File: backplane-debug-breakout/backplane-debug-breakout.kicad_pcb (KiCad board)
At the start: 2 copper layers, 11 parts, among them J1 Conn_02x08_Odd_Even, J2 Conn_01x04, J3 Conn_01x01_Socket, J4 Conn_01x01_Socket, J5 Conn_01x04, SW1 SW_Push, SW2 SW_DPST_x2

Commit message: added to pcb
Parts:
- moved SW2 43.7 mm to (136.0, 68.0)
- moved SW1 35.8 mm to (129.0, 69.4), turned to 90 degrees
- moved J2 15.9 mm to (115.0, 82.9)
- moved D1 12.7 mm to (118.8, 65.0)
- moved F2 12.5 mm to (118.5, 72.5)
- moved J5 8.65 mm to (109.8, 61.5), turned to -90 degrees
- moved J1 0.95 mm to (105.0, 70.2)
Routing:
- net /SD: track 0.71 -> 48.0 mm
- net /CAN_H: track 0.00 -> 17.5 mm
- net /OPD_SCL: track 0.00 -> 14.7 mm
- net Net-(D1-K): track 0.00 -> 13.4 mm
- net Net-(J1-Pin_10): track 0.00 -> 9.26 mm
- net /CAN_L: track 0.00 -> 8.82 mm
- added copper zone on B.Cu, net GND
- added copper zone on F.Cu, net GND

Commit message: updated pcb
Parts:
- moved PCB1 1.01 mm to (161.8, 62.0)
- moved vCAN 0.60 mm to (126.8, 105.4)
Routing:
- net /C3-UART-TX: track 0.00 -> 79.0 mm, vias 0 -> 1
- net /C3-UART-RX: track 0.00 -> 65.4 mm
- net Net-(D1-A): track 0.00 -> 42.7 mm, vias 0 -> 1
- net Net-(J1-Pin_10): track 9.26 -> 14.3 mm

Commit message: edited PBC
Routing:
- net Net-(PCB1-3V3): track 0.00 -> 2.54 mm
- net /C3-UART-TX: track 79.0 -> 80.6 mm
- net /C3-UART-RX: track 65.4 -> 66.4 mm
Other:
- board outline added: 65 x 50.5 mm
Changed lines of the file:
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@@
 		(tags "banana socket")
 		(property "Reference" "J4"
-			(at 0 -6.5 90)
+			(at 4 -5.5 90)
 			(layer "F.SilkS")
 			(effects
@@
 			)
 		)
-		(sheetname "Root")
-		(sheetfile "backplane-debug-breakout.kicad_sch")
 		(attr through_hole)
-		(fp_rect
-			(start 0 0)
+		(fp_line
+			(start 0 21)
 			(end 12.7 21)
 			(stroke
@@
 				(type default)
 			)
-			(fill none)
 			(layer "F.SilkS")
 		)
-		(fp_rect
-			(start 0 0)
-			(end 12.7 21)
+		(fp_line
+			(start 0 0.5)
+			(end 0 8)
 			(stroke
 				(width 0.1)
 				(type default)
 			)
-			(fill none)
-			(layer "F.CrtYd")
-		)
-		(fp_circle
-			(center 0 19.77)
-			(end 0.762 19.77)
-			(stroke
-				(width 0.05)
-				(type default)
-			)
-			(fill none)
-			(layer "F.CrtYd")
-		)
-		(fp_circle
-			(center 12.7 19.77)
-			(end 13.462 19.77)
-			(stroke
-				(width 0.05)
-				(type default)
-			)
-			(fill none)
-			(layer "F.CrtYd")
-		)
-		(fp_circle
-			(center 0 17.23)
-			(end 0.762 17.23)
-			(stroke
-				(width 0.05)
-				(type default)
-			)
-			(fill none)
-			(layer "F.CrtYd")
-		)
-		(fp_circle
-			(center 12.7 17.23)
-			(end 13.462 17.23)
-			(stroke
-				(width 0.05)
-				(type default)
-			)
-			(fill none)
-			(layer "F.CrtYd")
-		)
-		(fp_circle
-			(center 0 14.69)
-			(end 0.762 14.69)
-			(stroke
-				(width 0.05)
-				(type default)
-			)
-			(fill none)
-			(layer "F.CrtYd")
-		)
-		(fp_circle
-			(center 12.7 14.69)
-			(end 13.462 14.69)
-			(stroke
-				(width 0.05)
-				(type default)
-			)
-			(fill none)
-			(layer "F.CrtYd")
+			(layer "F.SilkS")
 		)
-		(fp_circle
-			(center 0 12.15)
-			(end 0.762 12.15)
+		(fp_line
+			(start 12.7 0.5)
+			(end 12.7 8)
 			(stroke
-				(width 0.05)
+				(width 0.1)
 				(type default)
 			)
-			(fill none)
-			(layer "F.CrtYd")
+			(layer "F.SilkS")
 		)
-		(fp_circle
-			(center 12.7 12.15)
-			(end 13.462 12.15)
+		(fp_line
+			(start 0 0)
+			(end 12.7 0)
 			(stroke
-				(width 0.05)
+				(width 0.1)
 				(type default)
 			)
-			(fill none)
-			(layer "F.CrtYd")
+			(layer "Cmts.User")
 		)
-		(fp_circle
-			(center 0 9.61)
-			(end 0.762 9.61)
+		(fp_rect
+			(start -2 -1)
+			(end 14.7 22)
 			(stroke
-				(width 0.05)
+				(width 0.1)
 				(type default)
 			)
@@
 			(layer "F.CrtYd")
 		)
-		(fp_circle
-			(center 12.7 9.61)
-			(end 13.462 9.61)
-			(stroke
-				(width 0.05)
-				(type default)
+		(fp_text user "PCB Edge"
+			(at 3.5 1.5 -90)
+			(unlocked yes)
+			(layer "Cmts.User")
+			(effects
+				(font
+					(size 1 1)
+					(thickness 0.15)
+				)
+				(justify left bottom)
 			)
-			(fill none)
-			(layer "F.CrtYd")
 		)
 		(fp_text user "${REFERENCE}"
@@
 			)
 		)
-		(pad "P1" thru_hole circle
+		(pad "P1" smd rect
 			(at 0 9.61 270)
-			(size 1.524 1.524)
-			(drill 0.762)
-			(layers "*.Cu" "*.Mask")
-			(remove_unused_layers no)
+			(size 2 2)
+			(layers "F.Cu" "F.Paste" "F.Mask")
 			(net 16 "unconnected-(PCB1-RESET#-PadP1)")
 			(pinfunction "RESET#")
 			(pintype "input+no_connect")
 		)
-		(pad "P2" thru_hole circle
+		(pad "P2" smd rect
 			(at 0 12.15 270)
-			(size 1.524 1.524)
-			(drill 0.762)
-			(layers "*.Cu" "*.Mask")
-			(remove_unused_layers no)
+			(size 2 2)
+			(layers "F.Cu" "F.Paste" "F.Mask")
 			(net 17 "Net-(PCB1-3V3)")
 			(pinfunction "3V3")
 			(pintype "power_out")
 		)
-		(pad "P3" thru_hole circle
+		(pad "P3" smd rect
 			(at 0 14.69 270)
-			(size 1.524 1.524)
-			(drill 0.762)
-			(layers "*.Cu" "*.Mask")
-			(remove_unused_layers no)
+			(size 2 2)
+			(layers "F.Cu" "F.Paste" "F.Mask")
 			(net 17 "Net-(PCB1-3V3)")
 			(pinfunction "VIO")
 			(pintype "power_in")
 		)
-		(pad "P4" thru_hole circle
+		(pad "P4" smd rect
 			(at 0 17.23 270)
-			(size 1.524 1.524)
-			(drill 0.762)
-			(layers "*.Cu" "*.Mask")
-			(remove_unused_layers no)
+			(size 2 2)
+			(layers "F.Cu" "F.Paste" "F.Mask")
 			(net 6 "GND")
 			(pinfunction "GND")
 			(pintype "power_in")
 		)
-		(pad "P5" thru_hole circle
+		(pad "P5" smd rect
 			(at 0 19.77 270)
-			(size 1.524 1.524)
-			(drill 0.762)
-			(layers "*.Cu" "*.Mask")
-			(remove_unused_layers no)
+			(size 2 2)
+			(layers "F.Cu" "F.Paste" "F.Mask")
 			(net 20 "unconnected-(PCB1-VBUS-PadP5)")
 			(pinfunction "VBUS")
 			(pintype "power_out+no_connect")
 		)
-		(pad "P6" thru_hole circle
+		(pad "P6" smd rect
 			(at 12.7 19.77 270)
-			(size 1.524 1.524)
-			(drill 0.762)
-			(layers "*.Cu" "*.Mask")
-			(remove_unused_layers no)
+			(size 2 2)
+			(layers "F.Cu" "F.Paste" "F.Mask")
 			(net 18 "unconnected-(PCB1-CB0-PadP6)")
 			(pinfunction "CB0")
 			(pintype "bidirectional+no_connect")
 		)
-		(pad "P7" thru_hole circle
+		(pad "P7" smd rect
 			(at 12.7 17.23 270)
-			(size 1.524 1.524)
-			(drill 0.762)
-			(layers "*.Cu" "*.Mask")
-			(remove_unused_layers no)
+			(size 2 2)
+			(layers "F.Cu" "F.Paste" "F.Mask")
 			(net 5 "/C3-UART-TX")
 			(pinfunction "TXD")
 			(pintype "output")
 		)
-		(pad "P8" thru_hole circle
+		(pad "P8" smd rect
 			(at 12.7 14.69 270)
-			(size 1.524 1.524)
-			(drill 0.762)
-			(layers "*.Cu" "*.Mask")
-			(remove_unused_layers no)
+			(size 2 2)
+			(layers "F.Cu" "F.Paste" "F.Mask")
 			(net 19 "unconnected-(PCB1-RTS#-PadP8)")
 			(pinfunction "RTS#")
 			(pintype "output+no_connect")
 		)
-		(pad "P9" thru_hole circle
+		(pad "P9" smd rect
 			(at 12.7 12.15 270)
-			(size 1.524 1.524)
-			(drill 0.762)
-			(layers "*.Cu" "*.Mask")
-			(remove_unused_layers no)
+			(size 2 2)
+			(layers "F.Cu" "F.Paste" "F.Mask")
 			(net 8 "/C3-UART-RX")
 			(pinfunction "RXD")
 			(pintype "input")
 		)
-		(pad "P10" thru_hole circle
+		(pad "P10" smd rect
 			(at 12.7 9.61 270)
-			(size 1.524 1.524)
-			(drill 0.762)
-			(layers "*.Cu" "*.Mask")
-			(remove_unused_layers no)
+			(size 2 2)
+			(layers "F.Cu" "F.Paste" "F.Mask")
 			(net 21 "unconnected-(PCB1-CTS#-PadP10)")
 			(pinfunction "CTS#")
@@
 		)
 	)
-	(gr_rect
-		(start 97 59)
-		(end 162 109.5)
-		(stroke
-			(width 0.2)
-			(type default)
-		)
-		(fill none)
-		(layer "F.Cu")
-		(net 4)
-	)
 	(gr_line
 		(start 114.96 82.92)
@@
 		(net 7)
 	)
+	(gr_rect
+		(start 97 59)
+		(end 162 109.5)
+		(stroke
+			(width 0.2)
+			(type default)
+		)
+		(fill none)
+		(layer "Edge.Cuts")
+	)
 	(segment
 		(start 113 65)
@@
 	(segment
 		(start 144.54 74.7)
-		(end 124.24 95)
+		(end 144.54 77.46)
 		(width 0.4)
 		(layer "F.Cu")
@@
 	)
 	(segment
-		(start 124.24 95)
+		(start 127 95)
 		(end 100.5 95)
 		(width 0.4)
@@
 		(net 5)
 	)
+	(segment
+		(start 144.54 77.46)
+		(end 127 95)
+		(width 0.4)
+		(layer "F.Cu")
+		(net 5)
+	)
 	(via
 		(at 100.5 73)
@@
 	)
 	(segment
-		(start 149.62 73.62)
-		(end 148.5 72.5)
+		(start 149.62 74.7)
+		(end 149.62 72.62)
 		(width 0.4)
 		(layer "F.Cu")
@@
 	)
 	(segment
-		(start 112 63.5)
-		(end 112 68.26)
+		(start 149 72)
+		(end 141.5 72)
 		(width 0.4)
 		(layer "F.Cu")
@@
 	)
 	(segment
-		(start 148.5 72.5)
-		(end 141 72.5)
+		(start 126.5 73)
+		(end 126.5 62)
 		(width 0.4)
 		(layer "F.Cu")
@@
 	)
 	(segment
-		(start 112 68.26)
-		(end 107.5 72.76)
+		(start 129 75.5)
+		(end 126.5 73)
 		(width 0.4)
 		(layer "F.Cu")
@@
 	)
 	(segment
-		(start 138 75.5)
-		(end 129 75.5)
+		(start 112 63.5)
+		(end 112 68.26)
 		(width 0.4)
 		(layer "F.Cu")
@@
 	)
 	(segment
-		(start 115 60.5)
-		(end 112 63.5)
+		(start 126.5 62)
+		(end 125 60.5)
 		(width 0.4)
 		(layer "F.Cu")
@@
 	)
 	(segment
-		(start 149.62 74.7)
-		(end 149.62 73.62)
+		(start 115 60.5)
+		(end 112 63.5)
 		(width 0.4)
 		(layer "F.Cu")
@@
 	)
 	(segment
-		(start 141 72.5)
-		(end 138 75.5)
+		(start 149.62 72.62)
+		(end 149 72)
 		(width 0.4)
 		(layer "F.Cu")
@@
 	)
 	(segment
-		(start 129 75.5)
-		(end 126.5 73)
+		(start 125 60.5)
+		(end 115 60.5)
 		(width 0.4)
 		(layer "F.Cu")
@@
 	)
 	(segment
-		(start 126.5 62)
-		(end 125 60.5)
+		(start 138 75.5)
+		(end 129 75.5)
 		(width 0.4)
 		(layer "F.Cu")
@@
 	)
 	(segment
-		(start 126.5 73)
-		(end 126.5 62)
+		(start 112 68.26)
+		(end 107.5 72.76)
 		(width 0.4)
 		(layer "F.Cu")
@@
 	)
 	(segment
-		(start 125 60.5)
-		(end 115 60.5)
+		(start 141.5 72)
+		(end 138 75.5)
 		(width 0.4)
 		(layer "F.Cu")
@@
 		(net 12)
 	)
+	(segment
+		(start 147.08 62)
+		(end 149.62 62)
+		(width 0.4)
+		(layer "F.Cu")
+		(net 17)
+	)
 	(zone

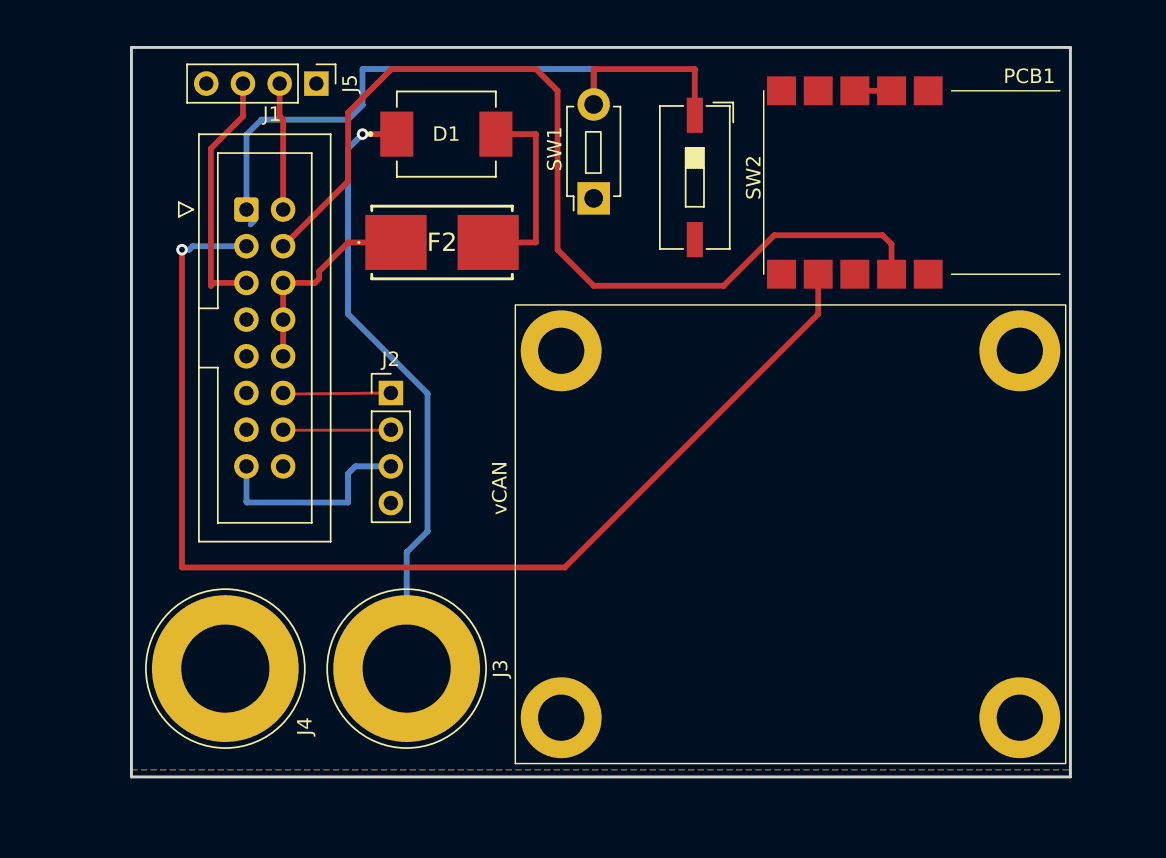
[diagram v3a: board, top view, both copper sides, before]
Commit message: added switches
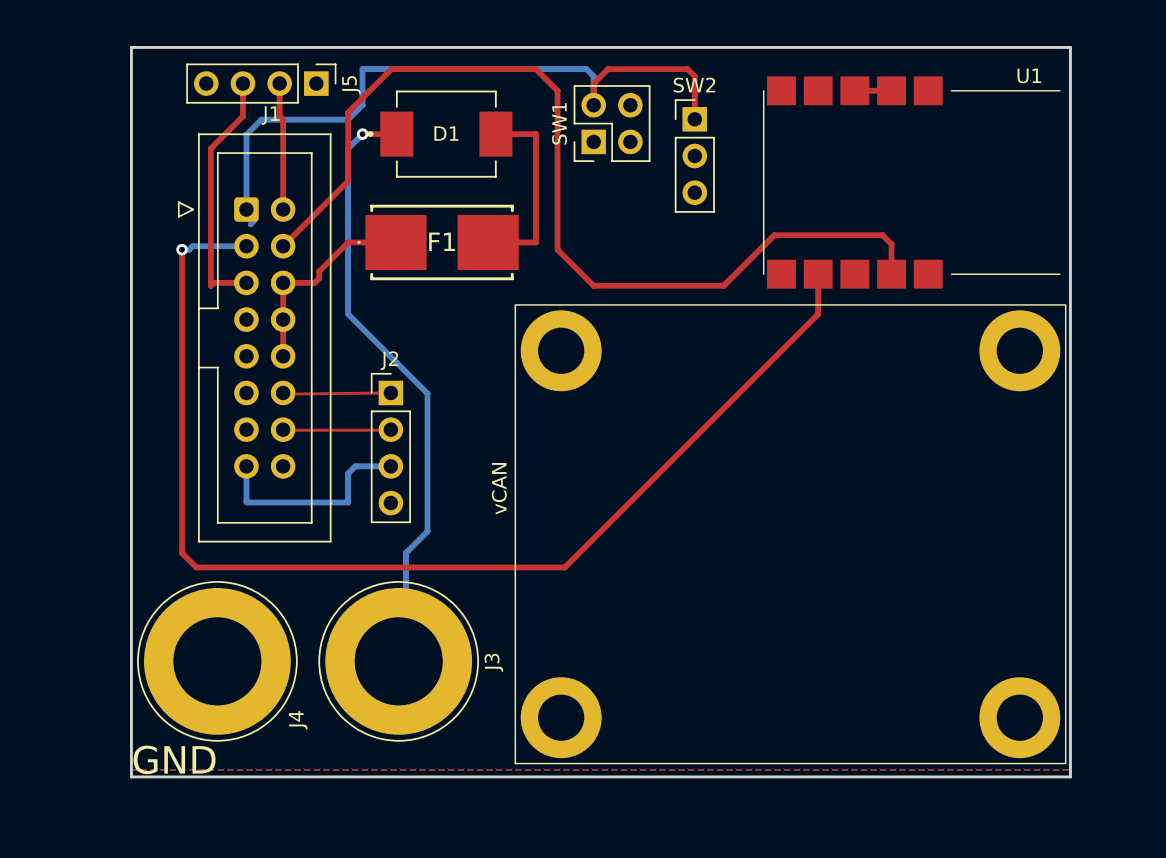
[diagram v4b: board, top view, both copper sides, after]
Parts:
- D1: value tbd -> TSM MURS315SH
- F1: renamed from F2; value Fuse_Small -> Fuseholder
- SW1: footprint Button_Switch_THT:SW_PUSH_1P1T_6x3.5mm_H4.3_APEM_MJTP1243 -> Connector_PinHeader_2.54mm:PinHeader_2x02_P2.54mm_Vertical
- SW2: footprint Button_Switch_SMD:SW_DIP_SPSTx01_Slide_9.78x4.72mm_W8.61mm_P2.54mm -> Connector_PinHeader_2.54mm:PinHeader_1x03_P2.54mm_Vertical
- moved SW2 4.02 mm to (136.0, 64.0), turned to 0 degrees
- moved SW1 3.90 mm to (129.0, 65.5)
- moved J3 0.74 mm to (115.5, 101.5)
- moved J4 0.74 mm to (103.0, 101.5)
- renumbered PCB1 to U1
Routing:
- net /SD: track 48.0 -> 47.1 mm
- net /C3-UART-TX: track 80.6 -> 80.0 mm
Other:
- board text added: "GND"

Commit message: modified pcb
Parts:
- removed SW1: SW_Push, Connector_PinHeader_2.54mm:PinHeader_2x02_P2.54mm_Vertical
- added SW3: EG1218, Connector_PinHeader_2.54mm:PinHeader_1x03_P2.54mm_Vertical, F.Cu at (135.0, 72.5)
- SW2: value SW_DPST_x2 -> SW_Omron_B3FS; footprint Connector_PinHeader_2.54mm:PinHeader_1x03_P2.54mm_Vertical -> Button_Switch_THT:SW_PUSH_6mm
- moved F1 5.31 mm to (116.0, 67.8), turned to 90 degrees
- moved D1 4.92 mm to (123.0, 67.6), turned to 90 degrees
- moved SW2 3.02 mm to (136.0, 67.0), turned to 180 degrees
- moved vCAN 0.65 mm to (127.0, 106.0)
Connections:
- net Net-(J1-Pin_10) renamed /VBUS
- SW2 pad 1: /SD -> GND
- SW2 pad 2: GND -> /SD
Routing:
- net Net-(D1-A): track 42.4 -> 34.3 mm, vias 1 -> 0
- net Net-(D1-K): track 13.4 -> 7.20 mm
- net /VBUS: track 14.3 -> 17.4 mm
- net /SD: track 47.1 -> 48.7 mm
- net /C3-UART-TX: track 80.0 -> 81.0 mm
- net GND: vias 0 -> 4
